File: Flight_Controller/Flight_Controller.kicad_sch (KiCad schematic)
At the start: 123 parts, among them IC1 ICM-20689, J1 USB_C_Receptacle_USB2.0_16P, J2 SM08B-SRSS-TB, J3 SM04B-SRSS-TB, J4 SM06B-SRSS-TBLFSN, J5 SM03B-SRSS-TB, Q1 AO3400A, SW1 SW_Push, U1 NO, U11 ESD224DQA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

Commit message: Primer Ruteo, capas externas
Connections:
- net ADC_CURR_IN: now also U9.4; no longer U12.4
- net ADC_CURR_OUT: now also U9.7; no longer U12.7
- net I2C_SCL_IN: now also U12.5; no longer U12.2
- net I2C_SCL_OUT: now also U12.6; no longer U12.9
- net I2C_SDA_IN: now also U12.4; no longer U12.1
- net I2C_SDA_OUT: now also U12.7; no longer U12.10
- net VIDEO_IN: now also U12.1; no longer U12.5
- net VIDEO_OUT: now also U12.10; no longer U12.6
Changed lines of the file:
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@@
 	)
 	(no_connect
-		(at 285.75 179.07)
-	)
-	(no_connect
 		(at 83.82 182.88)
 	)
@@
 	)
 	(no_connect
+		(at 285.75 200.66)
+	)
+	(no_connect
 		(at 226.06 110.49)
 	)
@@
 	)
 	(no_connect
+		(at 265.43 200.66)
+	)
+	(no_connect
 		(at 83.82 180.34)
 	)
@@
 		(at 22.86 189.23)
 	)
-	(no_connect
-		(at 265.43 179.07)
-	)
 	(wire
 		(pts
@@
 	(wire
 		(pts
+			(xy 285.75 179.07) (xy 287.02 179.07)
+		)
+		(stroke
+			(width 0)
+			(type default)
+		)
+	)
+	(wire
+		(pts
 			(xy 153.67 48.26) (xy 153.67 52.07)
 		)
@@
 	(wire
 		(pts
-			(xy 264.16 203.2) (xy 265.43 203.2)
-		)
-		(stroke
-			(width 0)
-			(type default)
-		)
-	)
-	(wire
-		(pts
 			(xy 285.75 106.68) (xy 287.02 106.68)
 		)
@@
 	(wire
 		(pts
-			(xy 264.16 200.66) (xy 265.43 200.66)
-		)
-		(stroke
-			(width 0)
-			(type default)
-		)
-	)
-	(wire
-		(pts
 			(xy 55.88 210.82) (xy 58.42 210.82)
 		)
@@
 	(wire
 		(pts
-			(xy 264.16 205.74) (xy 265.43 205.74)
+			(xy 375.92 168.91) (xy 378.46 168.91)
 		)
 		(stroke
@@
 	(wire
 		(pts
-			(xy 375.92 168.91) (xy 378.46 168.91)
+			(xy 261.62 233.68) (xy 264.16 233.68)
 		)
 		(stroke
@@
 	(wire
 		(pts
-			(xy 261.62 233.68) (xy 264.16 233.68)
+			(xy 285.75 157.48) (xy 287.02 157.48)
 		)
 		(stroke
@@
 	(wire
 		(pts
-			(xy 285.75 157.48) (xy 287.02 157.48)
+			(xy 285.75 173.99) (xy 287.02 173.99)
 		)
 		(stroke
@@
 	(wire
 		(pts
-			(xy 285.75 173.99) (xy 287.02 173.99)
+			(xy 33.02 91.44) (xy 44.45 91.44)
 		)
 		(stroke
@@
 	(wire
 		(pts
-			(xy 33.02 91.44) (xy 44.45 91.44)
+			(xy 212.09 254) (xy 215.9 254)
 		)
 		(stroke
@@
 	(wire
 		(pts
-			(xy 212.09 254) (xy 215.9 254)
+			(xy 264.16 205.74) (xy 265.43 205.74)
 		)
 		(stroke
@@
 	(wire
 		(pts
-			(xy 285.75 203.2) (xy 287.02 203.2)
-		)
-		(stroke
-			(width 0)
-			(type default)
-		)
-	)
-	(wire
-		(pts
 			(xy 55.88 30.48) (xy 67.31 30.48)
 		)
@@
 	(wire
 		(pts
-			(xy 285.75 198.12) (xy 287.02 198.12)
-		)
-		(stroke
-			(width 0)
-			(type default)
-		)
-	)
-	(wire
-		(pts
 			(xy 21.59 66.04) (xy 21.59 46.99)
 		)
@@
 	(wire
 		(pts
-			(xy 285.75 205.74) (xy 287.02 205.74)
+			(xy 177.8 156.21) (xy 171.45 156.21)
 		)
 		(stroke
@@
 	(wire
 		(pts
-			(xy 177.8 156.21) (xy 171.45 156.21)
+			(xy 171.45 49.53) (xy 171.45 60.96)
 		)
 		(stroke
@@
 	(wire
 		(pts
-			(xy 171.45 49.53) (xy 171.45 60.96)
+			(xy 264.16 203.2) (xy 265.43 203.2)
 		)
 		(stroke
@@
 	(wire
 		(pts
-			(xy 285.75 200.66) (xy 287.02 200.66)
-		)
-		(stroke
-			(width 0)
-			(type default)
-		)
-	)
-	(wire
-		(pts
 			(xy 332.74 57.15) (xy 339.09 57.15)
 		)
@@
 	(wire
 		(pts
+			(xy 285.75 205.74) (xy 287.02 205.74)
+		)
+		(stroke
+			(width 0)
+			(type default)
+		)
+	)
+	(wire
+		(pts
 			(xy 105.41 38.1) (xy 105.41 39.37)
 		)
@@
 	(wire
 		(pts
+			(xy 285.75 198.12) (xy 287.02 198.12)
+		)
+		(stroke
+			(width 0)
+			(type default)
+		)
+	)
+	(wire
+		(pts
 			(xy 332.74 53.34) (xy 332.74 57.15)
 		)
@@
 	(wire
 		(pts
-			(xy 264.16 198.12) (xy 265.43 198.12)
-		)
-		(stroke
-			(width 0)
-			(type default)
-		)
-	)
-	(wire
-		(pts
 			(xy 55.88 91.44) (xy 67.31 91.44)
 		)
@@
 	(wire
 		(pts
+			(xy 264.16 198.12) (xy 265.43 198.12)
+		)
+		(stroke
+			(width 0)
+			(type default)
+		)
+	)
+	(wire
+		(pts
 			(xy 320.04 31.75) (xy 320.04 34.29)
 		)
@@
 	(wire
 		(pts
+			(xy 285.75 203.2) (xy 287.02 203.2)
+		)
+		(stroke
+			(width 0)
+			(type default)
+		)
+	)
+	(wire
+		(pts
 			(xy 264.16 125.73) (xy 265.43 125.73)
 		)
@@
 	(wire
 		(pts
+			(xy 264.16 179.07) (xy 265.43 179.07)
+		)
+		(stroke
+			(width 0)
+			(type default)
+		)
+	)
+	(wire
+		(pts
 			(xy 55.88 64.77) (xy 55.88 66.04)
 		)
@@
 	(hierarchical_label "I2C_SDA_OUT"
 		(shape input)
-		(at 287.02 198.12 0)
+		(at 287.02 203.2 0)
 		(effects
 			(font
@@
 	(hierarchical_label "I2C_SDA_IN"
 		(shape input)
-		(at 264.16 198.12 180)
+		(at 264.16 203.2 180)
 		(effects
 			(font
@@
 	(hierarchical_label "ADC_CURR_OUT"
 		(shape input)
-		(at 287.02 203.2 0)
+		(at 287.02 179.07 0)
 		(effects
 			(font
@@
 	(hierarchical_label "ADC_CURR_IN"
 		(shape input)
-		(at 264.16 203.2 180)
+		(at 264.16 179.07 180)
 		(effects
 			(font
@@
 	(hierarchical_label "I2C_SCL_IN"
 		(shape input)
-		(at 264.16 200.66 180)
+		(at 264.16 205.74 180)
 		(effects
 			(font
@@
 	(hierarchical_label "I2C_SCL_OUT"
 		(shape input)
-		(at 287.02 200.66 0)
+		(at 287.02 205.74 0)
 		(effects
 			(font
@@
 	(hierarchical_label "VIDEO_IN"
 		(shape input)
-		(at 264.16 205.74 180)
+		(at 264.16 198.12 180)
 		(effects
 			(font
@@
 	(hierarchical_label "VIDEO_OUT"
 		(shape input)
-		(at 287.02 205.74 0)
+		(at 287.02 198.12 0)
 		(effects
 			(font

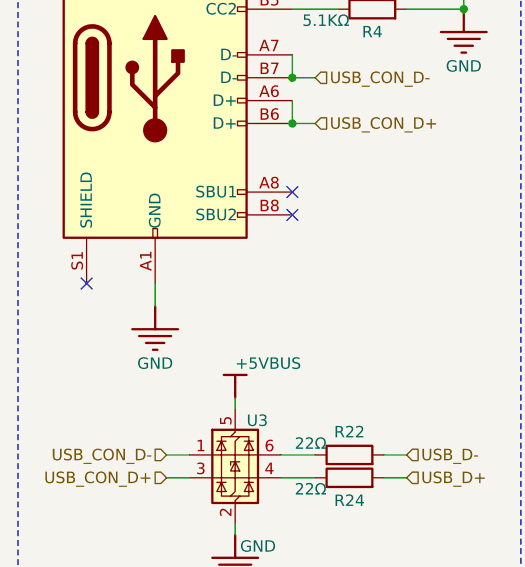
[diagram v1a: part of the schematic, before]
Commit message: Correccion ruteo, capa GND
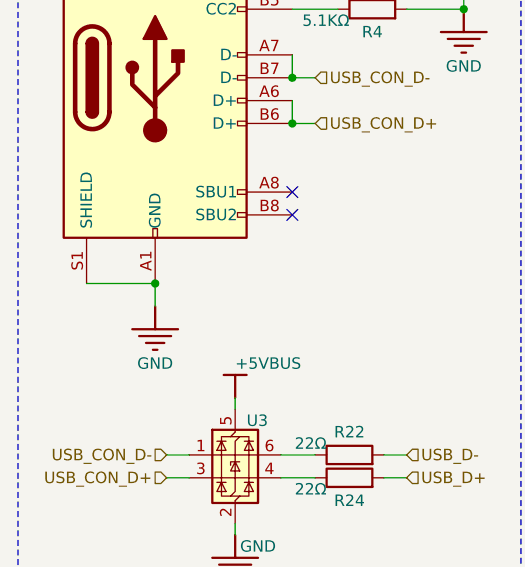
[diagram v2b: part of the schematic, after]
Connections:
- net GND: now also J1.S1 (SHIELD)
- no-connect marks 40 -> 39
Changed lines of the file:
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@@
+	)
+	(junction
+		(at 30.48 189.23)
+		(diameter 0)
+		(color 0 0 0 0)
 	)
 	(junction
@@
 		(at 226.06 85.09)
 	)
-	(no_connect
-		(at 22.86 189.23)
-	)
 	(wire
 		(pts
@@
 		)
 		(stroke
+			(width 0)
+			(type default)
+		)
+	)
+	(wire
+		(pts
+			(xy 22.86 189.23) (xy 30.48 189.23)
+		)
+		(stroke
